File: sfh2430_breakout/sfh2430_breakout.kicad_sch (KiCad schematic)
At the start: 22 parts, among them J1 Landing Pad, J2 Landing Pad, J3 Landing Pad, J4 Landing Pad, J5 Conn_01x10, U1 LTC2052IS_PBF

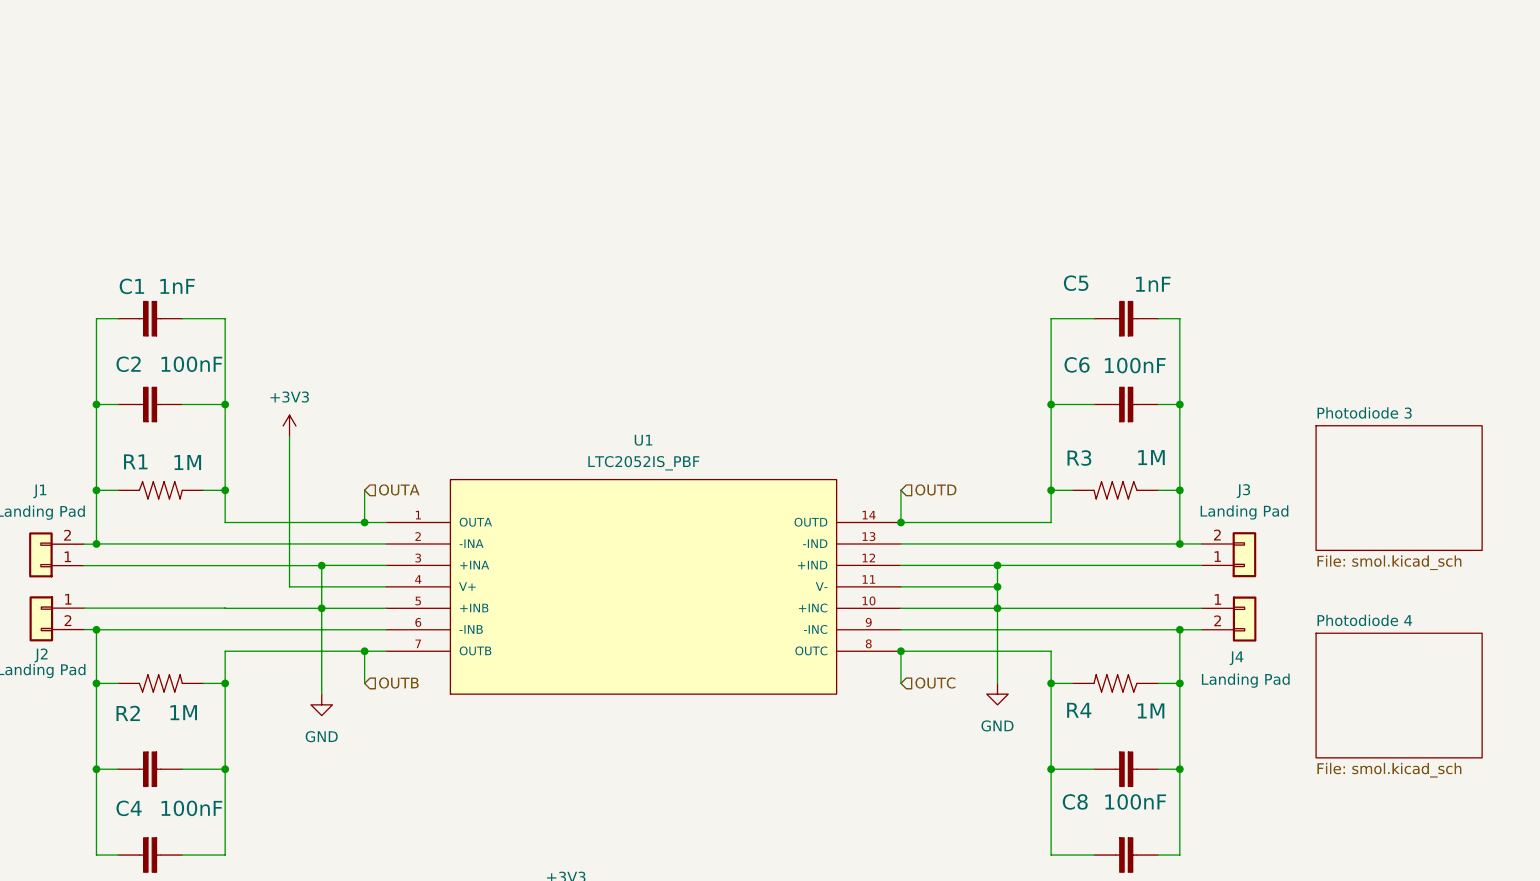
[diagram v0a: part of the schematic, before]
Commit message: add math and decals
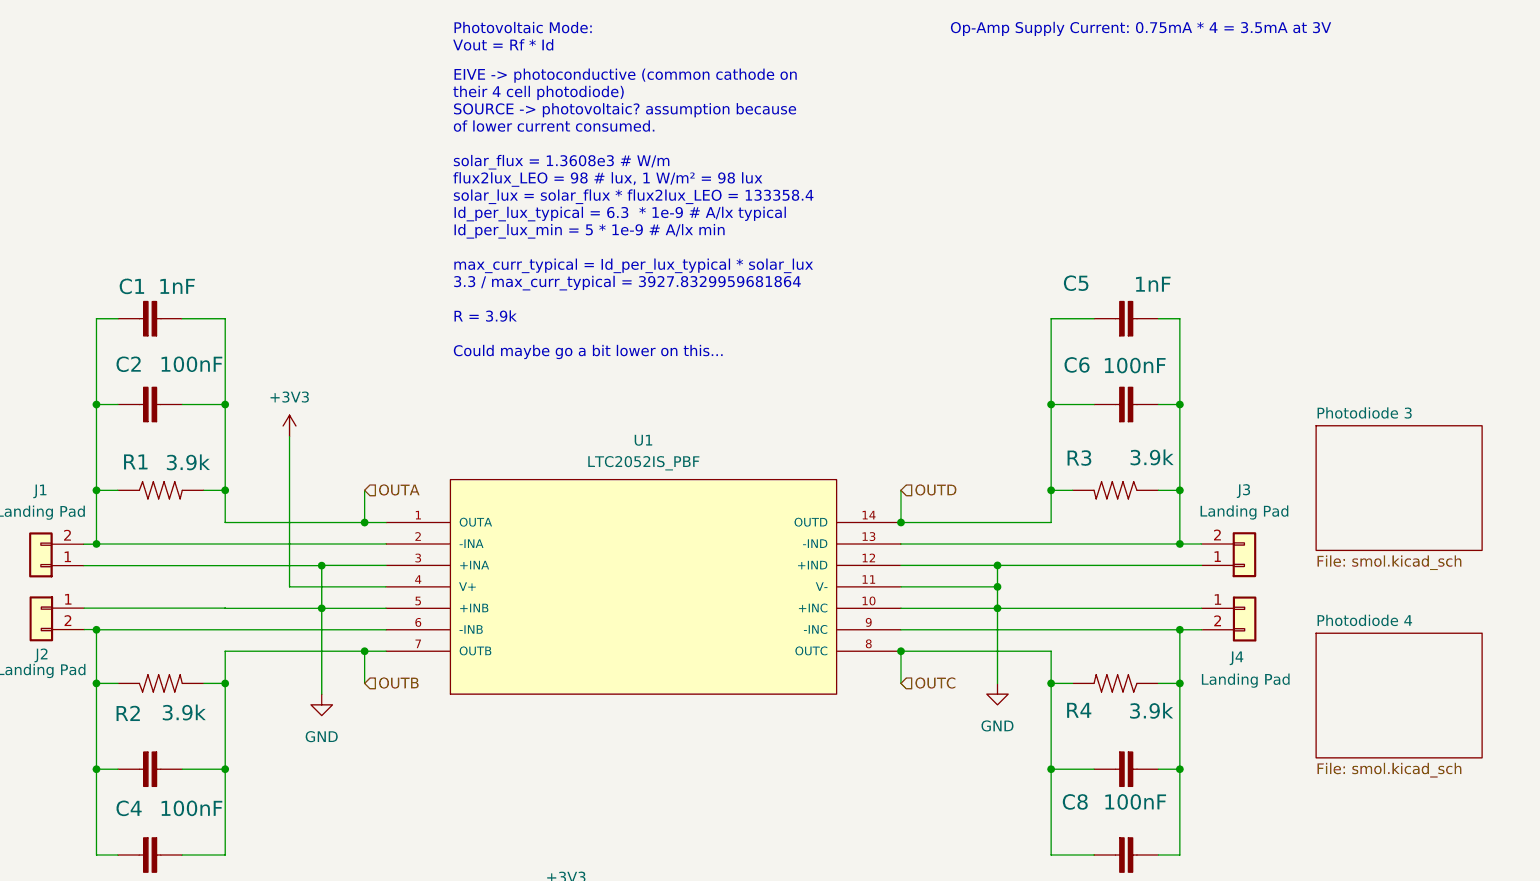
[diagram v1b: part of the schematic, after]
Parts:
- R1, R2, R3, R4: value 1M -> 3.9k
- U1: Availability In Stock -> (none); Check_prices https://www.snapeda.com/parts/LTC2052IS%23PBF/Analog+Device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 -> (none); MANUFACTURER_PART_NUMBER ltc2052is -> (none); MP LTC2052IS#PBF -> (none); Package SO-14 Linear Technology -> (none); Price None -> (none); Purchase-URL https://www.snapeda.com/api/url_track_click_mouser/?unipart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 -> (none); SnapEDA_Link https://www.snapeda.com/parts/LTC2052IS%23PBF/Analog+Device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 -> (none)
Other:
- note added: "EIVE -> photoconductive (common cathode on their 4 cell photodiode) SOURCE -> photovoltaic? assumption because of lower current consumed. solar_flux = 1.3608e3 # W/m flux2lux_LEO = 98 # lux, 1 W/m² = 98 lux solar_lux = solar_flux * flux2lux_LEO = 133358.4 Id_per_lux_typical = 6.3 * 1e-9 # A/lx typical Id_per_lux_min = 5 * 1e-9 # A/lx min max_curr_typical = Id_per_lux_typical * solar_lux 3.3 / max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"
- note added: "Op-Amp Supply Current: 0.75mA * 4 = 3.5mA at 3V"
- note added: "Photovoltaic Mode: Vout = Rf * Id"
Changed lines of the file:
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@@
     (stroke (width 0) (type default))
+  )
+  (text "EIVE -> photoconductive (common cathode on \ntheir 4 cell photodiode)\nSOURCE -> photovoltaic? assumption because \nof lower current consumed.\n\nsolar_flux = 1.3608e3 # W/m\nflux2lux_LEO = 98 # lux, 1 W/m² = 98 lux\nsolar_lux = solar_flux * flux2lux_LEO = 133358.4\nId_per_lux_typical = 6.3  * 1e-9 # A/lx typical\nId_per_lux_min = 5 * 1e-9 # A/lx min\n\nmax_curr_typical = Id_per_lux_typical * solar_lux\n3.3 / max_curr_typical = 3927.8329959681864\n\nR = 3.9k\n\nCould maybe go a bit lower on this..."
+    (at 122.2248 69.596 0)
+    (effects (font (size 1.27 1.27)) (justify left bottom))
   )
   (text "Mounting Holes" (at 16.6624 164.3634 0)
     (effects (font (size 2.159 2.159)) (justify left bottom))
+  )
+  (text "Photovoltaic Mode:\nVout = Rf * Id" (at 122.2248 33.401 0)
+    (effects (font (size 1.27 1.27)) (justify left bottom))
+  )
+  (text "Op-Amp Supply Current: 0.75mA * 4 = 3.5mA at 3V" (at 181.0766 31.3436 0)
+    (effects (font (size 1.27 1.27)) (justify left bottom))
   )
   (hierarchical_label "OUTD" (shape input) (at 144.5006 163.5252 180) (fields_autoplaced)
@@
       (effects (font (size 1.778 1.778)))
     )
-    (property "Value" "1M" (at 204.9018 81.28 0)
+    (property "Value" "3.9k" (at 204.9018 81.28 0)
       (effects (font (size 1.778 1.778)))
     )
@@
       (effects (font (size 1.778 1.778)))
     )
-    (property "Value" "1M" (at 90.805 81.8642 0)
+    (property "Value" "3.9k" (at 90.805 81.8642 0)
       (effects (font (size 1.778 1.778)))
     )
@@
       (effects (font (size 1.778 1.778)))
     )
-    (property "Value" "1M" (at 90.3224 111.4806 0)
+    (property "Value" "3.9k" (at 90.3224 111.4806 0)
       (effects (font (size 1.778 1.778)))
     )
@@
       (effects (font (size 1.27 1.27)) (justify bottom) hide)
     )
-    (property "Datasheet" "" (at 114.3 88.9 0)
+    (property "Datasheet" "https://www.analog.com/media/en/technical-documentation/data-sheets/20512fd.pdf" (at 114.3 88.9 0)
       (effects (font (size 1.27 1.27)) hide)
     )
@@
     )
     (property "Description" "\nLinear IC - Op-amp Linear Technology LTC2052IS#PBF Scrambler (zero drift) SO 14\n" (at 114.3 77.47 0)
-      (effects (font (size 1.27 1.27)) (justify bottom) hide)
-    )
-    (property "Package" "SO-14 Linear Technology" (at 114.3 74.93 0)
-      (effects (font (size 1.27 1.27)) (justify bottom) hide)
-    )
-    (property "Price" "None" (at 113.03 78.74 0)
-      (effects (font (size 1.27 1.27)) (justify bottom) hide)
-    )
-    (property "Check_prices" "https://www.snapeda.com/parts/LTC2052IS%23PBF/Analog+Devices/view-part/?ref=eda" (at 114.3 74.93 0)
-      (effects (font (size 1.27 1.27)) (justify bottom) hide)
-    )
-    (property "SnapEDA_Link" "https://www.snapeda.com/parts/LTC2052IS%23PBF/Analog+Devices/view-part/?ref=snap" (at 114.3 69.85 0)
-      (effects (font (size 1.27 1.27)) (justify bottom) hide)
-    )
-    (property "MP" "LTC2052IS#PBF" (at 114.3 77.47 0)
-      (effects (font (size 1.27 1.27)) (justify bottom) hide)
-    )
-    (property "Purchase-URL" "https://www.snapeda.com/api/url_track_click_mouser/?unipart_id=619050&manufacturer=Analog Devices&part_name=LTC2052IS#PBF&search_term=None" (at 114.3 74.93 0)
-      (effects (font (size 1.27 1.27)) (justify bottom) hide)
-    )
-    (property "Availability" "In Stock" (at 114.3 81.28 0)
-      (effects (font (size 1.27 1.27)) (justify bottom) hide)
-    )
-    (property "MANUFACTURER_PART_NUMBER" "ltc2052is" (at 114.3 72.39 0)
       (effects (font (size 1.27 1.27)) (justify bottom) hide)
     )
@@
       (effects (font (size 1.778 1.778)))
     )
-    (property "Value" "1M" (at 204.851 111.2774 0)
+    (property "Value" "3.9k" (at 204.851 111.2774 0)
       (effects (font (size 1.778 1.778)))
     )

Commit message: sfh2400 v2 (flex PCB)
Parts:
- removed C1, C3, C5, C7: 1nF, Capacitor_SMD:C_0603_1608Metric, symbol mainboard:22UF-1210-16V-20%
- removed C2, C4, C6, C8: 100nF, Capacitor_SMD:C_0603_1608Metric, symbol mainboard:22UF-1210-16V-20%
- removed J1, J2, J3, J4: Landing Pad, adcs:photodiode_landing_pad, symbol Connector_Generic:Conn_01x02
- removed J5: Conn_01x10, Connector_PinHeader_2.54mm:PinHeader_1x10_P2.54mm_Vertical, symbol Connector_Generic:Conn_01x10
- removed R1, R2, R3, R4: 3.9k, Resistor_SMD:R_0603_1608Metric, symbol pycubed_mainboard:RESISTOR0603
- added J1: Conn_01x06, sapling:MOLEX_2053380006, symbol solar-panel-side-Y-plus-rescue:2053380006-sapling
- H1, H2, H3, H4: footprint MountingHole:MountingHole_3.2mm_M3_DIN965_Pad -> MountingHole:MountingHole_2.2mm_M2_DIN965_Pad_TopBottom; DNI DNI -> (none); now left out of the parts list
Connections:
- net +3V3: now also J1.6
- net GND: now also J1.1
- net Photodiode 3/IN-: now reaches U1.9 (-INC)
- net Photodiode 4/IN-: now reaches U1.13 (-IND)
- net Photodiode 1/IN-: now reaches U1.2 (-INA)
- net Photodiode 2/IN-: now reaches U1.6 (-INB)
- net OUTA renamed OUT1
- net OUT1: now also J1.3
- net OUTB renamed OUT2
- net OUT2: now also J1.2
- net OUTC renamed OUT3
- net OUT3: now also J1.5
- net OUTD renamed OUT4
- net OUT4: now also J1.4
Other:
- sheet Photodiode 1 ports: added IN+, IN-, OUT; removed none
- sheet Photodiode 2 ports: added IN+, IN-, OUT; removed none
- sheet Photodiode 3 ports: added IN+, IN-, OUT; removed none
- sheet Photodiode 4 ports: added IN+, IN-, OUT; removed none

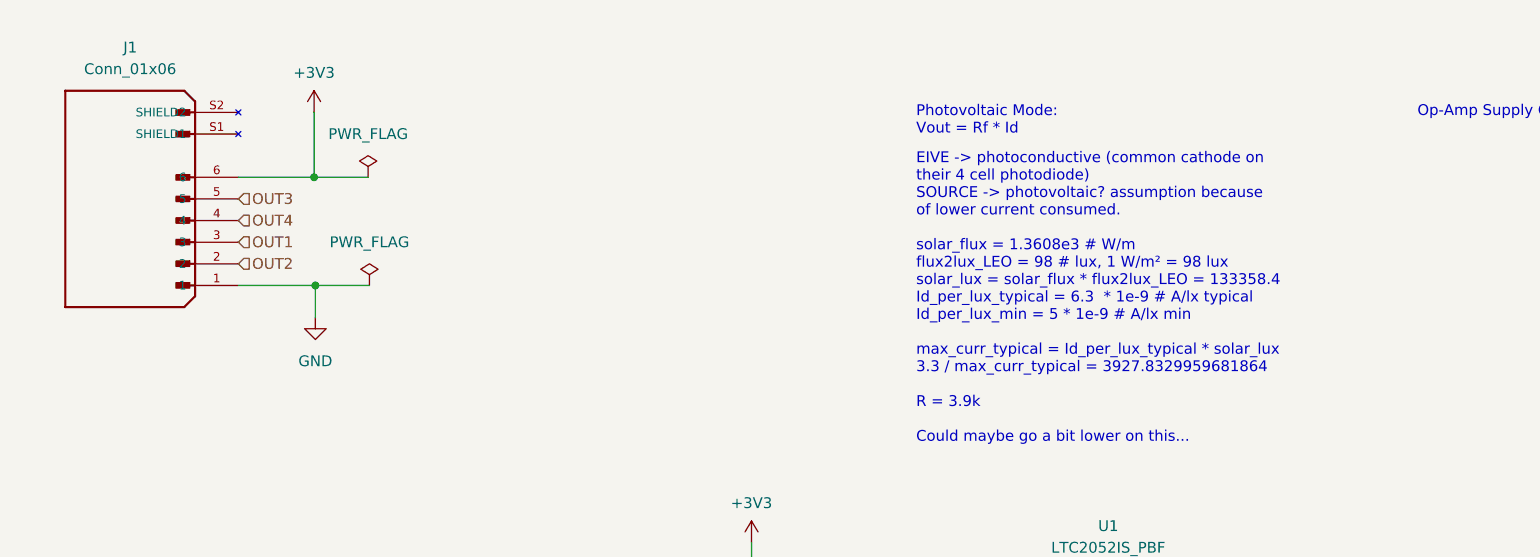
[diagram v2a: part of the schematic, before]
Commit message: ffc/fpc pyramid
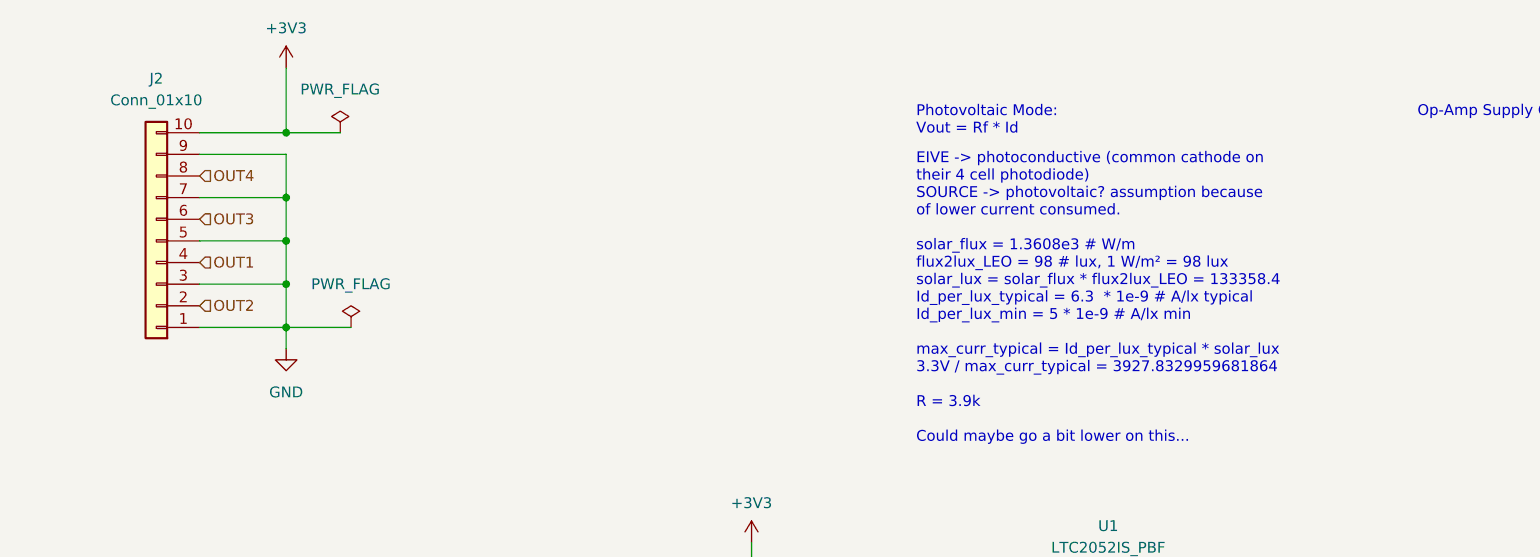
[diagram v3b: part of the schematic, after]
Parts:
- removed J1: Conn_01x06, sapling:MOLEX_2053380006, symbol solar-panel-side-Y-plus-rescue:2053380006-sapling
- added J2: Conn_01x10, adcs:10pin_1mm_pitch_flat_flex, symbol Connector_Generic:Conn_01x10
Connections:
- net +3V3: now also J2.10 (Pin_10)
- net GND: now also J2.1 (Pin_1), J2.3 (Pin_3), J2.5 (Pin_5), J2.7 (Pin_7), J2.9 (Pin_9)
- net OUT1: now also J2.4 (Pin_4)
- net OUT2: now also J2.2 (Pin_2)
- net OUT3: now also J2.6 (Pin_6)
- net OUT4: now also J2.8 (Pin_8)
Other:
- note added: "EIVE -> photoconductive (common cathode on their 4 cell photodiode) SOURCE -> photovoltaic? assumption because of lower current consumed. solar_flux = 1.3608e3 # W/m flux2lux_LEO = 98 # lux, 1 W/m² = 98 lux solar_lux = solar_flux * flux2lux_LEO = 133358.4 Id_per_lux_typical = 6.3 * 1e-9 # A/lx typical Id_per_lux_min = 5 * 1e-9 # A/lx min max_curr_typical = Id_per_lux_typical * solar_lux 3.3V / ma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"
- note removed: "EIVE -> photoconductive (common cathode on their 4 cell photodiode) SOURCE -> photovoltaic? assumption because of lower current consumed. solar_flux = 1.3608e3 # W/m flux2lux_LEO = 98 # lux, 1 W/m² = 98 lux solar_lux = solar_flux * flux2lux_LEO = 133358.4 Id_per_lux_typical = 6.3 * 1e-9 # A/lx typical Id_per_lux_min = 5 * 1e-9 # A/lx min max_curr_typical = Id_per_lux_typical * solar_lux 3.3 / max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"

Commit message: work on sun pyramid
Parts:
- H1, H2, H3, H4: footprint MountingHole:MountingHole_2.2mm_M2_DIN965_Pad_TopBottom -> MountingHole:MountingHole_2.2mm_M2
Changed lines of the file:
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@@
       (effects (font (size 1.27 1.27)) (justify left))
     )
-    (property "Footprint" "MountingHole:MountingHole_2.2mm_M2_DIN965_Pad_TopBottom" (at 19.1008 171.5516 0)
+    (property "Footprint" "MountingHole:MountingHole_2.2mm_M2" (at 19.1008 171.5516 0)
       (effects (font (size 1.27 1.27)) hide)
     )
@@
       (effects (font (size 1.27 1.27)) (justify left))
     )
-    (property "Footprint" "MountingHole:MountingHole_2.2mm_M2_DIN965_Pad_TopBottom" (at 43.2308 186.7916 0)
+    (property "Footprint" "MountingHole:MountingHole_2.2mm_M2" (at 43.2308 186.7916 0)
       (effects (font (size 1.27 1.27)) hide)
     )
@@
       (effects (font (size 1.27 1.27)) (justify left))
     )
-    (property "Footprint" "MountingHole:MountingHole_2.2mm_M2_DIN965_Pad_TopBottom" (at 43.2308 171.5516 0)
+    (property "Footprint" "MountingHole:MountingHole_2.2mm_M2" (at 43.2308 171.5516 0)
       (effects (font (size 1.27 1.27)) hide)
     )
@@
       (effects (font (size 1.27 1.27)) (justify left))
     )
-    (property "Footprint" "MountingHole:MountingHole_2.2mm_M2_DIN965_Pad_TopBottom" (at 19.1008 186.7916 0)
-      (effects (font (size 1.27 1.27)) hide)
-    )
+    (property "Footprint" "MountingHole:MountingHole_2.2mm_M2" (at 19.1008 186.7916 0)
+      (effects (font (size 1.27 1.27)) hide)
+    )
